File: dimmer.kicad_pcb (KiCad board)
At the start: 2 copper layers, 25 x 49.5 mm, 38 parts, among them J1 Conn_01x02, J2 Conn_01x02, J3 Conn_01x05, J4 Conn_01x06, Q1 HY1503C1, Q2 HY1503C1, Q3 HY1503C1, Q4 HY1503C1, Q5 HY1503C1, U1 L78M05ABDT-TR, U2 AMS1117-3.3, U3 ESP-12F, U4 SN74AVC8T245PW

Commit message: Switch to buck & go to production!
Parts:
- added C10: 10u, Capacitor_SMD:C_0402_1005Metric, F.Cu at (105.8, 55.0)
- added C11: 10u, Capacitor_SMD:C_0402_1005Metric, F.Cu at (106.1, 56.5)
- added C12: 100n, Capacitor_SMD:C_0402_1005Metric, F.Cu at (108.8, 56.5)
- added L1: 15uH 750mA, Inductor_SMD:L_Bourns-SRN4018, F.Cu at (108.8, 53.8)
- added R15: 51k, Resistor_SMD:R_0402_1005Metric, F.Cu at (105.7, 60.5)
- added R16: 10k, Resistor_SMD:R_0402_1005Metric, F.Cu at (105.7, 61.5)
- J4: footprint Connector_PinHeader_2.54mm:PinHeader_1x06_P2.54mm_Horizontal -> Library:PinHeader_1x06_P2.54mm_Horizontal
- U1: value L78M05ABDT-TR -> RY8310; footprint Package_TO_SOT_SMD:TO-252-2 -> Package_TO_SOT_SMD:TSOT-23-6
- moved J1 6.45 mm to (115.1, 71.2), turned to 180 degrees
- moved JP1 5.80 mm to (108.6, 63.7), turned to 180 degrees
- moved C3 5.50 mm to (111.2, 59.5)
- moved C2 2.93 mm to (105.6, 57.9), turned to 90 degrees
- moved C1 2.61 mm to (110.8, 61.5), turned to 0 degrees
- moved U1 2.02 mm to (108.8, 58.8), turned to 0 degrees
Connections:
- C3 pad 1: +5V -> VCC
- U1 pad 1: GND -> Net-(C12-Pad1)
- U1 pad 2: +5V -> GND
- U1 pad 3: VCC -> Net-(R15-Pad2)
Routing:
- net GND: track 32.1 -> 44.5 mm, vias 52 -> 59
- net VCC: track 10.4 -> 18.9 mm
- net +5V: track 35.0 -> 40.1 mm
- net Net-(R15-Pad2): track 0.00 -> 2.31 mm
- net Net-(C12-Pad1): track 0.00 -> 1.56 mm
- added copper zone on F.Cu, net Net-(C12-Pad2)

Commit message: Simplify design
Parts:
- removed C8, C9: 100n, Capacitor_SMD:C_0402_1005Metric
- removed J3: Conn_01x05, Connector_PinHeader_1.27mm:PinHeader_1x05_P1.27mm_Vertical
- removed U4: SN74AVC8T245PW, Package_SO:TSSOP-24_4.4x7.8mm_P0.65mm
- added Q10: WNM2030, Package_TO_SOT_SMD:SOT-723, F.Cu at (97.0, 70.4)
- added Q6: WNM2030, Package_TO_SOT_SMD:SOT-723, F.Cu at (113.0, 70.4)
- added Q7: WNM2030, Package_TO_SOT_SMD:SOT-723, F.Cu at (109.0, 70.4)
- added Q8: WNM2030, Package_TO_SOT_SMD:SOT-723, F.Cu at (105.0, 70.4)
- added Q9: WNM2030, Package_TO_SOT_SMD:SOT-723, F.Cu at (101.0, 70.4)
- J1: footprint Connector_PinHeader_2.54mm:PinHeader_1x02_P2.54mm_Vertical -> Connector_Wire:SolderWire-1sqmm_1x02_P5.4mm_D1.4mm_OD2.7mm
- R10, R11, R12, R13, R9: value 100 -> 2.4k
- moved R3 6.51 mm to (116.6, 49.5)
- moved R6 5.00 mm to (104.9, 69.0), turned to 180 degrees
- moved R7 5.00 mm to (100.9, 69.0), turned to 180 degrees
- moved R8 5.00 mm to (96.9, 69.0), turned to 180 degrees
- moved R5 4.99 mm to (109.0, 69.0), turned to 180 degrees
- moved R4 4.99 mm to (113.0, 69.0), turned to 180 degrees
- moved J1 4.86 mm to (116.0, 66.4), turned to 90 degrees
- moved R11 3.84 mm to (106.4, 70.3)
- moved R10 3.83 mm to (110.4, 70.3)
- moved R12 3.83 mm to (102.4, 70.3)
- moved R13 3.83 mm to (98.4, 70.3)
- moved R9 3.83 mm to (114.4, 70.3)
- moved J4 3.18 mm to (113.5, 77.4)
- moved LOGO1 3.18 mm to (115.2, 72.3)
- moved Q1 3.18 mm to (114.5, 73.4)
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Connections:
- C4 pad 1: +3V3 -> +3.3V
- C6 pad 1: +3V3 -> +3.3V
- C7 pad 1: +3V3 -> +3.3V
- R10 pad 1: Net-(R10-Pad1) -> +5V
- R11 pad 1: Net-(R11-Pad1) -> +5V
- R12 pad 1: Net-(R12-Pad1) -> +5V
- R13 pad 1: Net-(R13-Pad1) -> +5V
- R14 pad 1: +3V3 -> +3.3V
- R2 pad 1: +3V3 -> +3.3V
- R3 pad 1: +3V3 -> +3.3V
- R4 pad 1: Net-(R4-Pad1) -> +3.3V
- R4 pad 2: GND -> /CH0_D
- R5 pad 1: Net-(R10-Pad1) -> +3.3V
- R5 pad 2: GND -> /CH1_D
- R6 pad 1: Net-(R11-Pad1) -> +3.3V
- R6 pad 2: GND -> /CH2_D
- R7 pad 1: Net-(R12-Pad1) -> +3.3V
- R7 pad 2: GND -> /CH3_D
- R8 pad 1: Net-(R13-Pad1) -> +3.3V
- R8 pad 2: GND -> /CH4_D
- R9 pad 1: Net-(R4-Pad1) -> +5V
- U2 pad 2: +3V3 -> +3.3V
- U3 pad 17: /CH4_D -> /CH0_D
- U3 pad 4: /CH0_D -> /CH3_D
- U3 pad 5: /CH1_D -> /CH4_D
- U3 pad 7: /CH3_D -> /CH1_D
- U3 pad 8: +3V3 -> +3.3V
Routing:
- net +3V3: track 81.9 -> 0.00 mm, vias 4 -> 0
- net +3.3V: track 0.00 -> 73.1 mm, vias 0 -> 4
- net /TX: track 31.6 -> 0.00 mm
- net /RX: track 28.4 -> 0.00 mm
- net /CH0_D: track 34.1 -> 56.8 mm
- net GND: track 44.5 -> 22.7 mm, vias 59 -> 42
- net /GPIO0: track 25.9 -> 7.40 mm, vias 2 -> 0
- net Net-(R13-Pad1): track 14.1 -> 0.00 mm
- net Net-(R4-Pad1): track 12.4 -> 0.00 mm
- net /CH4_D: track 40.7 -> 30.3 mm, vias 0 -> 2
- net Net-(R10-Pad1): track 9.99 -> 0.00 mm
- net Net-(R12-Pad1): track 9.74 -> 0.00 mm
- net /CH3_D: track 26.0 -> 35.1 mm, vias 0 -> 4
- net +5V: track 40.1 -> 48.0 mm, vias 1 -> 8
- net Net-(R11-Pad1): track 6.99 -> 0.00 mm
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- added copper zone on F.Cu, net +3.3V
- removed copper zone on F.Cu, net +3V3
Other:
- board size 25 x 49.5 mm -> 25 x 46.3 mm

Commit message: reannotate
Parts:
- renumbered C5 to C1, C1 to C10, C7 to C2, C6 to C3, C10 to C4, C11 to C5, C12 to C6, C2 to C7, C3 to C8, C4 to C9, J2 to J1, J1 to J2, J4 to J3, Q10 to Q1, Q1 to Q10, Q9 to Q2, Q8 to Q3, Q7 to Q4, Q6 to Q5, Q5 to Q6, Q4 to Q7, Q3 to Q8, Q2 to Q9, R2 to R1, R5 to R10, R4 to R11, R13 to R12, R12 to R13, R11 to R14, R10 to R15, R9 to R16, R3 to R2, R14 to R3, R1 to R4, R15 to R5, R16 to R6, R8 to R7, R7 to R8, R6 to R9, U3 to U1, U1 to U3

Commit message: Disconnect CH0 from on-board LED
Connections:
- U1 pad 17: /CH0_D -> unconnected-(U1-Pad17)
- U1 pad 19: unconnected-(U3-Pad19) -> /CH0_D
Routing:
- net /CH0_D: track 56.8 -> 58.1 mm

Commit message: Increase 3.3V regulator pad size
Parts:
- J2: footprint Connector_Wire:SolderWire-1sqmm_1x02_P5.4mm_D1.4mm_OD2.7mm -> Connector_Wire:SolderWire-0.75sqmm_1x02_P4.8mm_D1.25mm_OD2.3mm
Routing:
- net GND: track 22.7 -> 24.2 mm, vias 42 -> 36

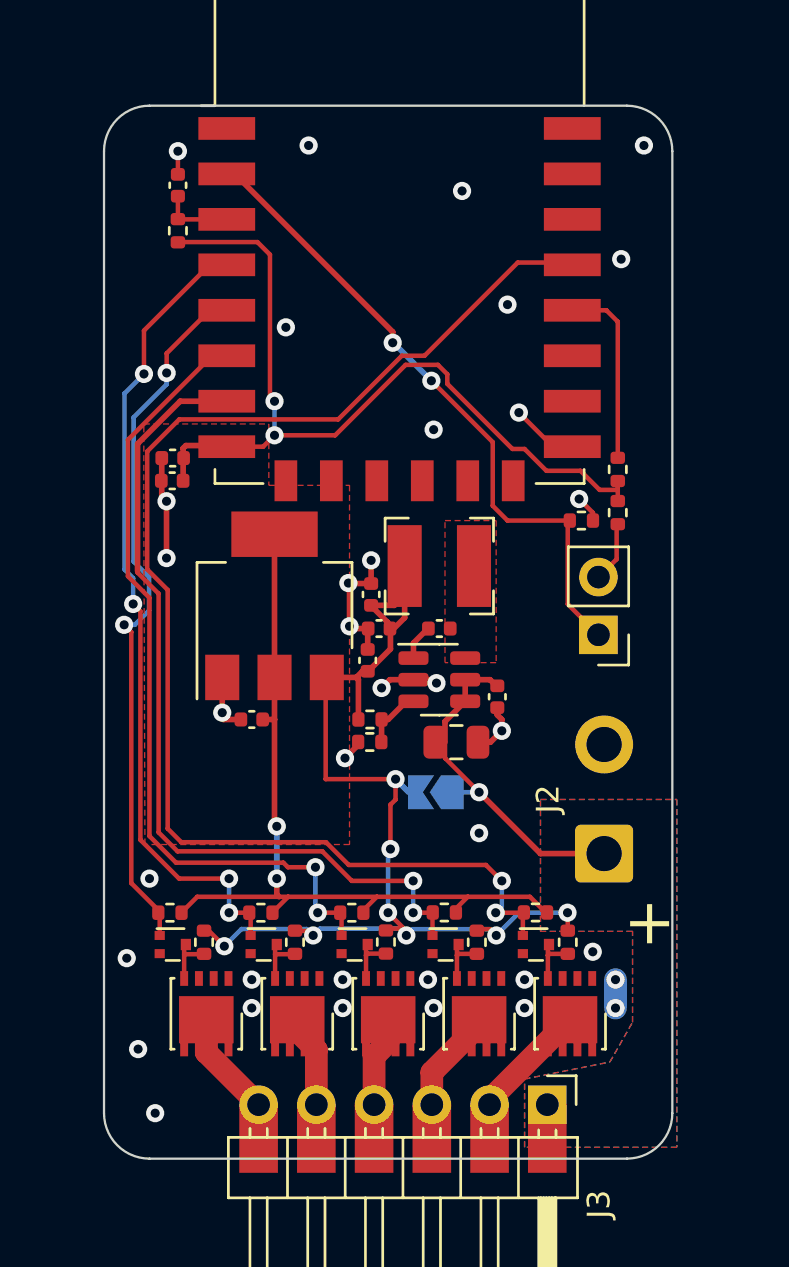
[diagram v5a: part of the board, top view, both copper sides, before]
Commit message: Add tooling holes
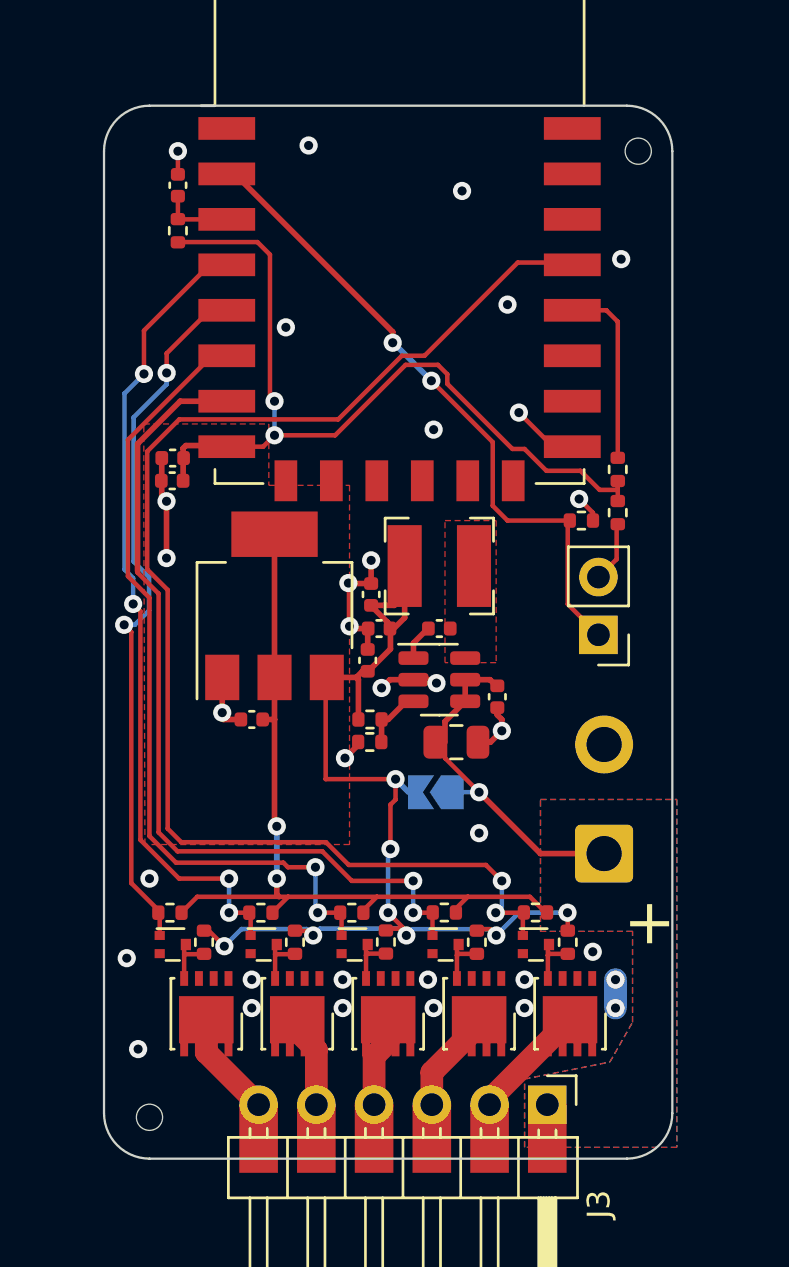
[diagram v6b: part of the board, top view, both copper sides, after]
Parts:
- added H1: MountingHole, Library:ToolingHole, F.Cu at (117.5, 35.5)
- added H2: MountingHole, Library:ToolingHole, F.Cu at (96.0, 78.0)
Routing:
- net GND: vias 36 -> 34
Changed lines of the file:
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@@
   (net 36 "unconnected-(U1-Pad17)")
   (net 37 "unconnected-(U1-Pad20)")
+  (footprint "Library:ToolingHole" (layer "F.Cu")
+    (at 96 78)
+    (property "Sheetfile" "dimmer.kicad_sch")
+    (property "Sheetname" "")
+    (property "exclude_from_bom" "")
+    (attr through_hole)
+    (fp_text reference "H2" (at 0 -0.5 unlocked) (layer "F.SilkS") hide
+      (effects (font (size 1 1) (thickness 0.15)))
+    )
+    (fp_text value "MountingHole" (at 0 1 unlocked) (layer "F.Fab")
+      (effects (font (size 1 1) (thickness 0.15)))
+    )
+    (pad "" np_thru_hole circle (at 0 0) (size 1.152 1.152) (drill 1.152) (layers F&B.Cu *.Mask)
+      (clearance 0.148))
+  )
   (footprint "Capacitor_SMD:C_0402_1005Metric" (layer "F.Cu")
     (at 105.6 57.9 90)
@@
     )
   )
+  (footprint "Library:ToolingHole" (layer "F.Cu")
+    (at 117.5 35.5)
+    (property "Sheetfile" "dimmer.kicad_sch")
+    (property "Sheetname" "")
+    (property "exclude_from_bom" "")
+    (attr through_hole)
+    (fp_text reference "H1" (at 0 -0.5 unlocked) (layer "F.SilkS") hide
+      (effects (font (size 1 1) (thickness 0.15)))
+    )
+    (fp_text value "MountingHole" (at 0 1 unlocked) (layer "F.Fab")
+      (effects (font (size 1 1) (thickness 0.15)))
+    )
+    (pad "" np_thru_hole circle (at 0 0) (size 1.152 1.152) (drill 1.152) (layers F&B.Cu *.Mask)
+      (clearance 0.148))
+  )
   (footprint "Library:DFN-8-1EP_3x3mm_P0.65mm_EP2x2.4mm" (layer "F.Cu")
     (at 114.5 73.44375 -90)
@@
     (property "Sheetname" "")
     (attr exclude_from_pos_files)
-    (fp_text reference "J2" (at 2.4 -2.47 90) (layer "F.SilkS")
+    (fp_text reference "J2" (at 2.4 -2.47 90) (layer "F.SilkS") hide
       (effects (font (size 1 1) (thickness 0.15)))
     )
@@
   (via (at 95 71) (size 0.8) (drill 0.4) (layers "F.Cu" "B.Cu") (free) (net 2))
   (via (at 106.210416 59.114049) (size 0.8) (drill 0.4) (layers "F.Cu" "B.Cu") (net 2))
-  (via (at 117.75 35.25) (size 0.8) (drill 0.4) (layers "F.Cu" "B.Cu") (free) (net 2))
   (via (at 112.5 73.19375) (size 0.8) (drill 0.4) (layers "F.Cu" "B.Cu") (free) (net 2))
   (via (at 96.75 50.9) (size 0.8) (drill 0.4) (layers "F.Cu" "B.Cu") (net 2))
@@
   (via (at 116.75 40.25) (size 0.8) (drill 0.4) (layers "F.Cu" "B.Cu") (free) (net 2))
   (via (at 100.5 71.94375) (size 0.8) (drill 0.4) (layers "F.Cu" "B.Cu") (free) (net 2))
-  (via (at 96.25 77.81875) (size 0.8) (drill 0.4) (layers "F.Cu" "B.Cu") (free) (net 2))
   (via (at 116.5 71.94375) (size 0.8) (drill 0.4) (layers "F.Cu" "B.Cu") (free) (net 2))
   (via (at 103 35.25) (size 0.8) (drill 0.4) (layers "F.Cu" "B.Cu") (free) (net 2))
